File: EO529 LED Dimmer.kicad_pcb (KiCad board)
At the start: 2 copper layers, 77.5 x 58.4 mm, 59 parts, among them J1 VBat, Q1 BC639, Q2 BC639, Q3 BC639, Q4 BC639, U1 NE556, U2 NE556, U3 LM393, U4 LM393

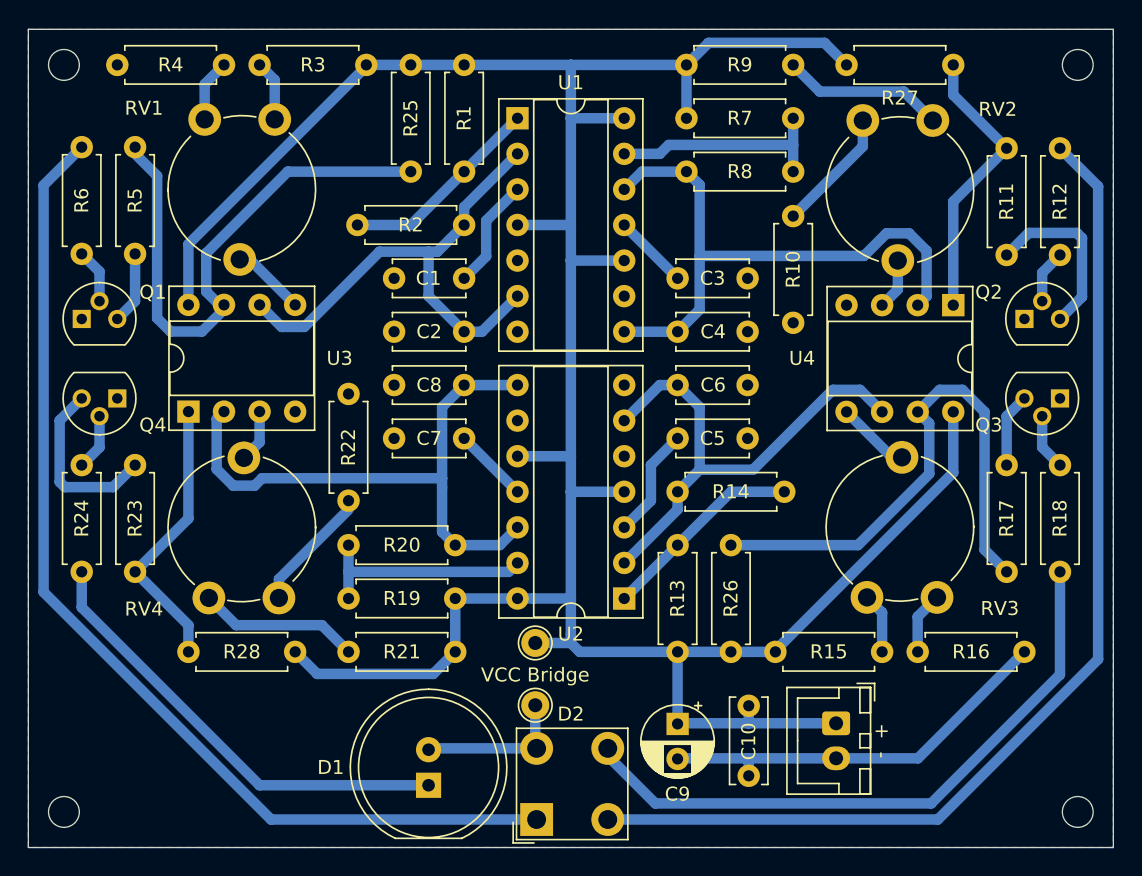
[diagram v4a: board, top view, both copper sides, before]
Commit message: Revert "Updated working design"
This reverts commit 5c7890285543894d12d83f256540f6246ef53dc3.
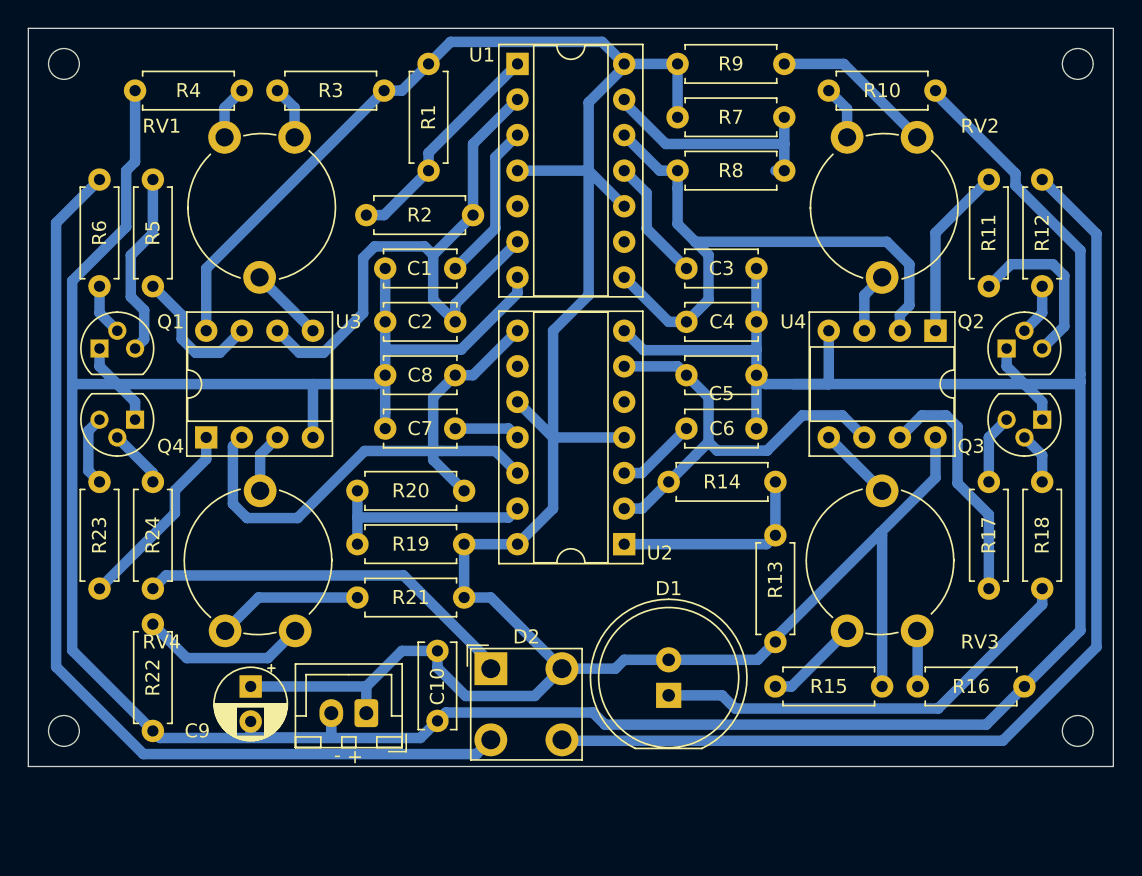
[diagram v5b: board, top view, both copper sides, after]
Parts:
- removed R25, R26, R27, R28: 1M, Resistor_THT:R_Axial_DIN0207_L6.3mm_D2.5mm_P7.62mm_Horizontal
- removed TP1, TP2: TestPoint, TestPoint:TestPoint_THTPad_D2.0mm_Drill1.0mm
- R10, R15, R16, R21, R22, R3, R4, R9: value 82k -> 100k
- R24: value 180 -> 150
- R6: value 150 -> 220
- moved J1 33.6 mm to (88.9, 118.1), turned to 180 degrees
- moved C9 30.6 mm to (80.6, 116.2)
- moved C10 22.6 mm to (94.0, 113.7)
- moved D1 18.3 mm to (110.5, 116.8)
- moved R22 16.5 mm to (73.7, 111.8), turned to 270 degrees
- moved D2 11.3 mm to (97.8, 114.9), turned to 0 degrees
- moved R10 9.31 mm to (121.9, 73.7), turned to 0 degrees
- moved R15 8.01 mm to (125.7, 116.2), turned to 180 degrees
- moved R13 7.02 mm to (118.1, 113.0)
- moved H2 5.78 mm to (67.3, 119.4)
- moved H4 5.78 mm to (139.7, 119.4)
- moved R5 5.46 mm to (73.7, 80.0), turned to 270 degrees
- moved R24 5.22 mm to (73.7, 101.6)
- moved R19 3.93 mm to (95.9, 106.0)
- moved R20 3.93 mm to (88.3, 102.2)
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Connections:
- D1 pad 1: Net-(R24-Pad2) -> Net-(D1-Pad1)
- D1 pad 2: V_LED -> VCC
- D2 pad 4: V_LED -> VCC
- R12 pad 2: Green -> Blue
- R18 pad 2: Blue -> Net-(D1-Pad1)
- R24 pad 2: Net-(R24-Pad2) -> Red
- R6 pad 2: Red -> Green
- U1 pad 5: unconnected-(U1-Pad5) -> Net-(U1-Pad5)
- U1 pad 9: unconnected-(U1-Pad9) -> Net-(U1-Pad9)
- U2 pad 5: unconnected-(U2-Pad5) -> Net-(U2-Pad5)
- U2 pad 9: unconnected-(U2-Pad9) -> Net-(U2-Pad9)
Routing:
- net GND: track 29.2 -> 285.7 mm
- net Red: track 74.8 -> 27.5 mm
- net Net-(R24-Pad2): track 32.6 -> 0.00 mm
- net Net-(D1-Pad1): track 0.00 -> 31.3 mm
- net Blue: track 45.4 -> 75.9 mm
- net Net-(R5-Pad2): track 39.8 -> 9.96 mm
- net Net-(R17-Pad2): track 39.2 -> 17.6 mm
- net V_LED: track 10.9 -> 0.00 mm
- net VCC: track 204.5 -> 194.7 mm
- net Net-(Q1-Pad3): track 5.17 -> 13.4 mm
- net Net-(R11-Pad2): track 20.3 -> 12.4 mm
- net Net-(Q4-Pad3): track 12.8 -> 5.11 mm
- net Net-(C2-Pad1): track 36.6 -> 44.1 mm
- net Green: track 77.4 -> 70.1 mm
- net Net-(R23-Pad2): track 20.0 -> 14.0 mm
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- removed copper zone on B.Cu, net GND
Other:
- board size 77.5 x 58.4 mm -> 77.5 x 52.7 mm
- net class Default added: clearance 0.4, trace_width 0.75, via_dia 0.8, via_drill 0.4
- rule pad_to_mask_clearance: 0 -> 0.05
- board text removed: "VCC Bridge"
